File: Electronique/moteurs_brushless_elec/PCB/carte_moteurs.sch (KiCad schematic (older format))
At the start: 0 parts

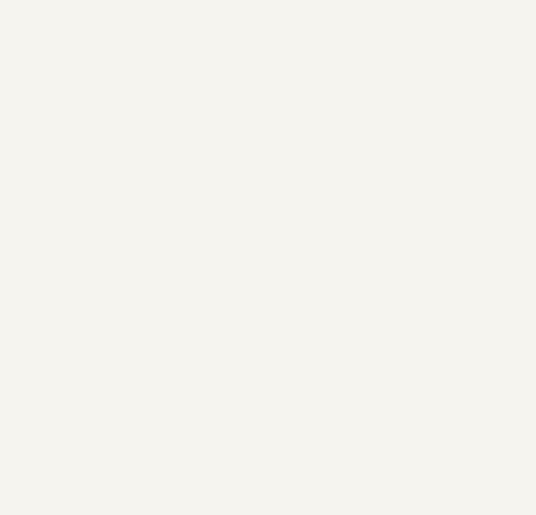
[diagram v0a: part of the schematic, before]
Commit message: rectification des empreintes
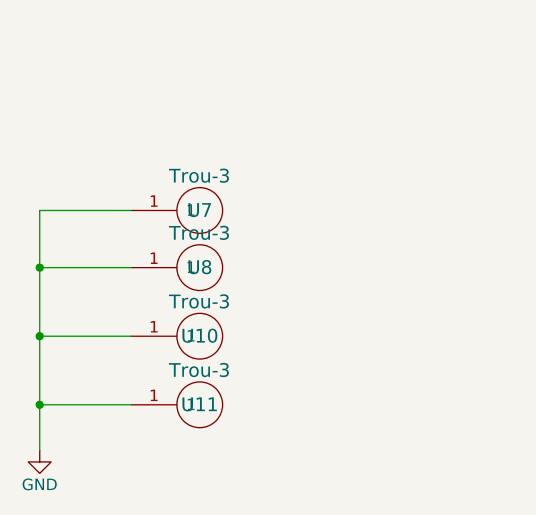
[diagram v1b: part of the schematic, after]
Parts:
- added U10, U11, U7, U8: Trou-3, maxon:Trou-3, symbol Trou-3
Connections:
- new net GND: U10.1, U11.1, U7.1, U8.1
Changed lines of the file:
@@
 Wire Wire Line
 	7650 2600 6650 2600
+$Comp
+L Trou-3 U7
+U 1 1 5A340DE3
+P 2000 4150
+F 0 "U7" H 2000 4150 60  0000 C CNN
+F 1 "Trou-3" H 2000 4300 60  0000 C CNN
+F 2 "maxon:Trou-3" H 2000 4150 60  0001 C CNN
+F 3 "" H 2000 4150 60  0000 C CNN
+	1    2000 4150
+	1    0    0    -1
+$EndComp
+$Comp
+L Trou-3 U8
+U 1 1 5A340F1E
+P 2000 4400
+F 0 "U8" H 2000 4400 60  0000 C CNN
+F 1 "Trou-3" H 2000 4550 60  0000 C CNN
+F 2 "maxon:Trou-3" H 2000 4400 60  0001 C CNN
+F 3 "" H 2000 4400 60  0000 C CNN
+	1    2000 4400
+	1    0    0    -1
+$EndComp
+$Comp
+L Trou-3 U10
+U 1 1 5A340FE1
+P 2000 4700
+F 0 "U10" H 2000 4700 60  0000 C CNN
+F 1 "Trou-3" H 2000 4850 60  0000 C CNN
+F 2 "maxon:Trou-3" H 2000 4700 60  0001 C CNN
+F 3 "" H 2000 4700 60  0000 C CNN
+	1    2000 4700
+	1    0    0    -1
+$EndComp
+$Comp
+L Trou-3 U11
+U 1 1 5A3410AC
+P 2000 5000
+F 0 "U11" H 2000 5000 60  0000 C CNN
+F 1 "Trou-3" H 2000 5150 60  0000 C CNN
+F 2 "maxon:Trou-3" H 2000 5000 60  0001 C CNN
+F 3 "" H 2000 5000 60  0000 C CNN
+	1    2000 5000
+	1    0    0    -1
+$EndComp
+$Comp
+L GND #PWR1
+U 1 1 5A34117D
+P 1300 5200
+F 0 "#PWR1" H 1300 4950 50  0001 C CNN
+F 1 "GND" H 1300 5050 50  0000 C CNN
+F 2 "" H 1300 5200 50  0000 C CNN
+F 3 "" H 1300 5200 50  0000 C CNN
+	1    1300 5200
+	1    0    0    -1
+$EndComp
+Wire Wire Line
+	1700 4150 1300 4150
+Wire Wire Line
+	1300 4150 1300 5200
+Wire Wire Line
+	1700 4400 1300 4400
+Connection ~ 1300 4400
+Wire Wire Line
+	1700 4700 1300 4700
+Connection ~ 1300 4700
+Wire Wire Line
+	1700 5000 1300 5000
+Connection ~ 1300 5000
 $EndSCHEMATC
